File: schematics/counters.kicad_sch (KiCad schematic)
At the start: 44 parts, among them Q1 2N2222, U1 74HC14, U10 74HC390, U3 74HC86, U31 74HC08, U32 74HC32, U33 74HC08, U4 74HC4046, U5 74HC390, U6 74HC390, U7 74HC390, U8 LMC555xN, U9 74HC390

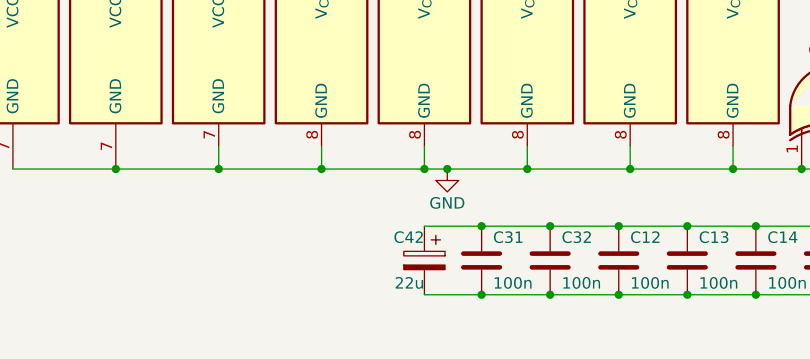
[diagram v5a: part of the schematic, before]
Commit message: revert to toroid inductor
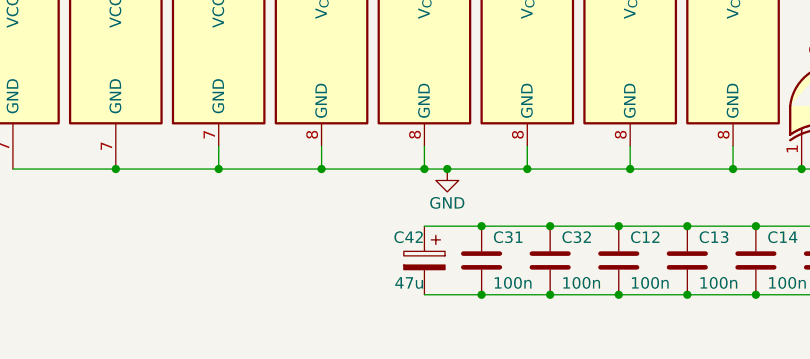
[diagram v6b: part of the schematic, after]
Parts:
- C42: value 22u -> 47u
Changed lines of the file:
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@@
 			)
 		)
-		(property "Value" "22u"
+		(property "Value" "47u"
 			(at 63.5 196.85 0)
 			(show_name no)
